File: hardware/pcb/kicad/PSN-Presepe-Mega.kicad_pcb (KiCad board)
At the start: 2 copper layers, 280 x 170 mm, 77 parts, among them J1 12V_IN, K1 G5Q-1_DC12, K10 G5Q-1_DC12, K11 G5Q-1_DC12, K12 G5Q-1_DC12, K13 G5Q-1_DC12, K14 G5Q-1_DC12, K15 G5Q-1_DC12, K16 G5Q-1_DC12, K2 G5Q-1_DC12, K3 G5Q-1_DC12, K4 G5Q-1_DC12, K5 G5Q-1_DC12, K6 G5Q-1_DC12, K7 G5Q-1_DC12, K8 G5Q-1_DC12, K9 G5Q-1_DC12, Q1 IRLZ44N_CIELO_R, Q2 IRLZ44N_CIELO_G, Q3 IRLZ44N_CIELO_B, Q4 IRLZ44N_TRAM_R, Q5 IRLZ44N_TRAM_G, Q6 IRLZ44N_TRAM_B, Q7 IRLZ44N_ALBA_R, Q8 IRLZ44N_ALBA_G, Q9 IRLZ44N_ALBA_B, U1 ULN2803C, U2 ULN2803C

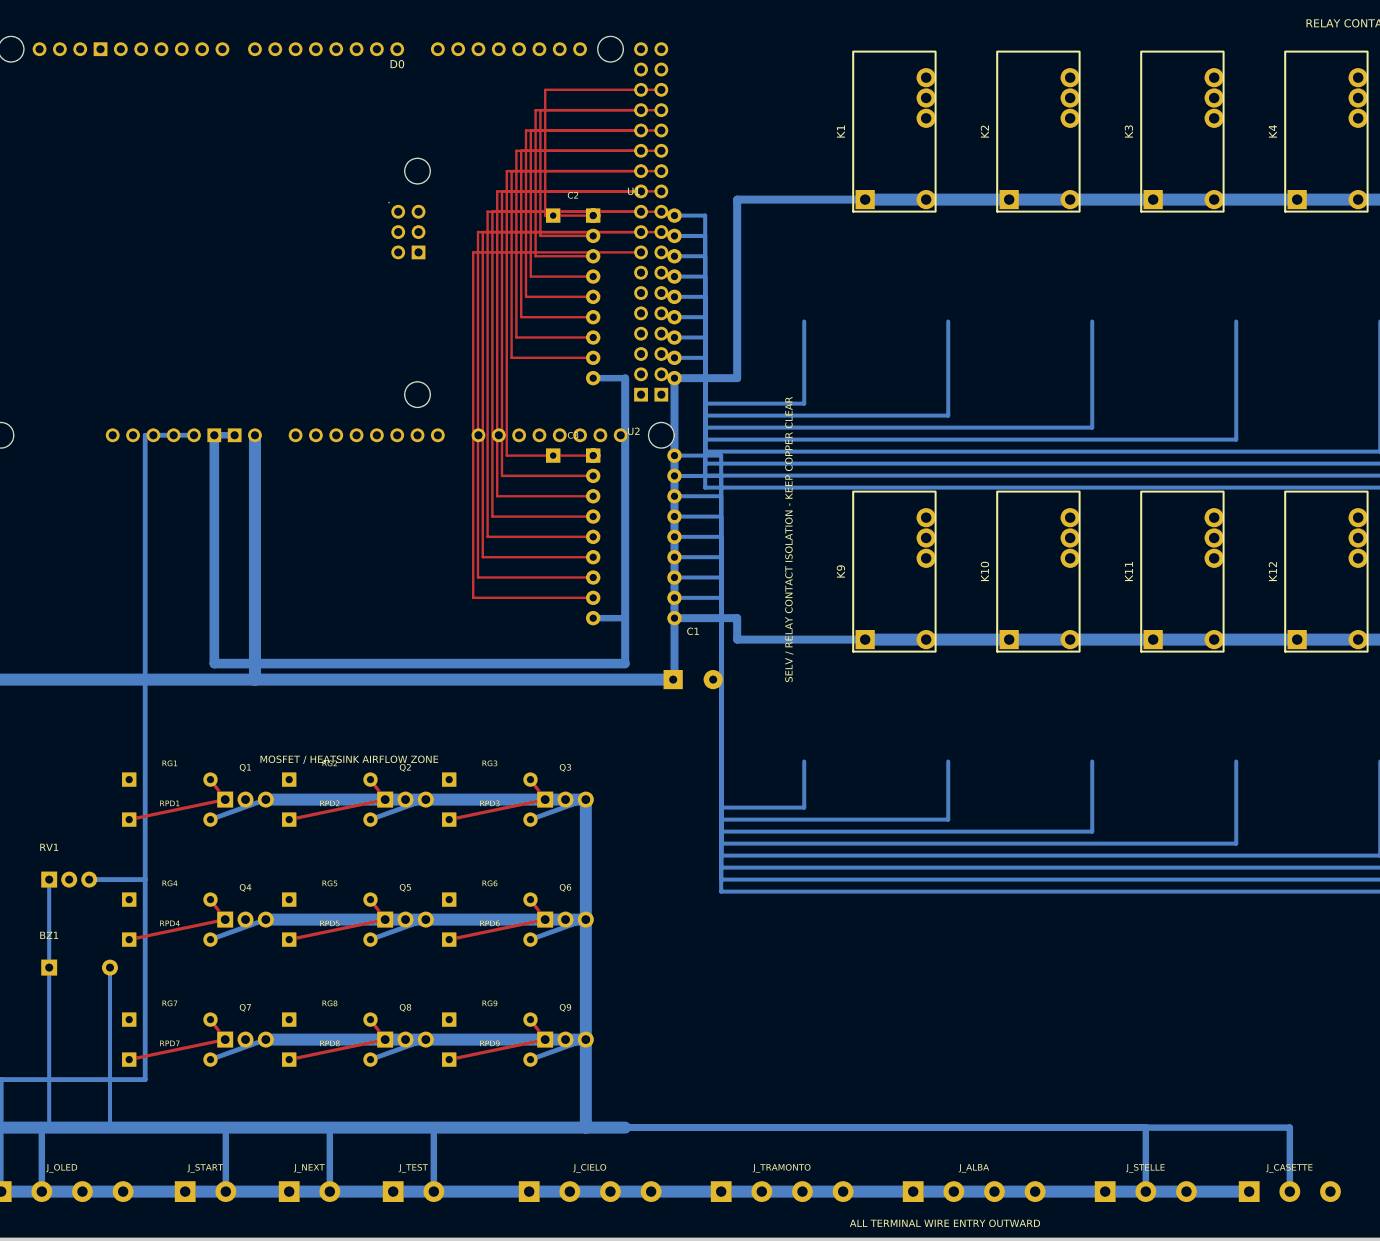
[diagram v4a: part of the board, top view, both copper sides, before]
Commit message: Route low-voltage controls and RGB PWM signals
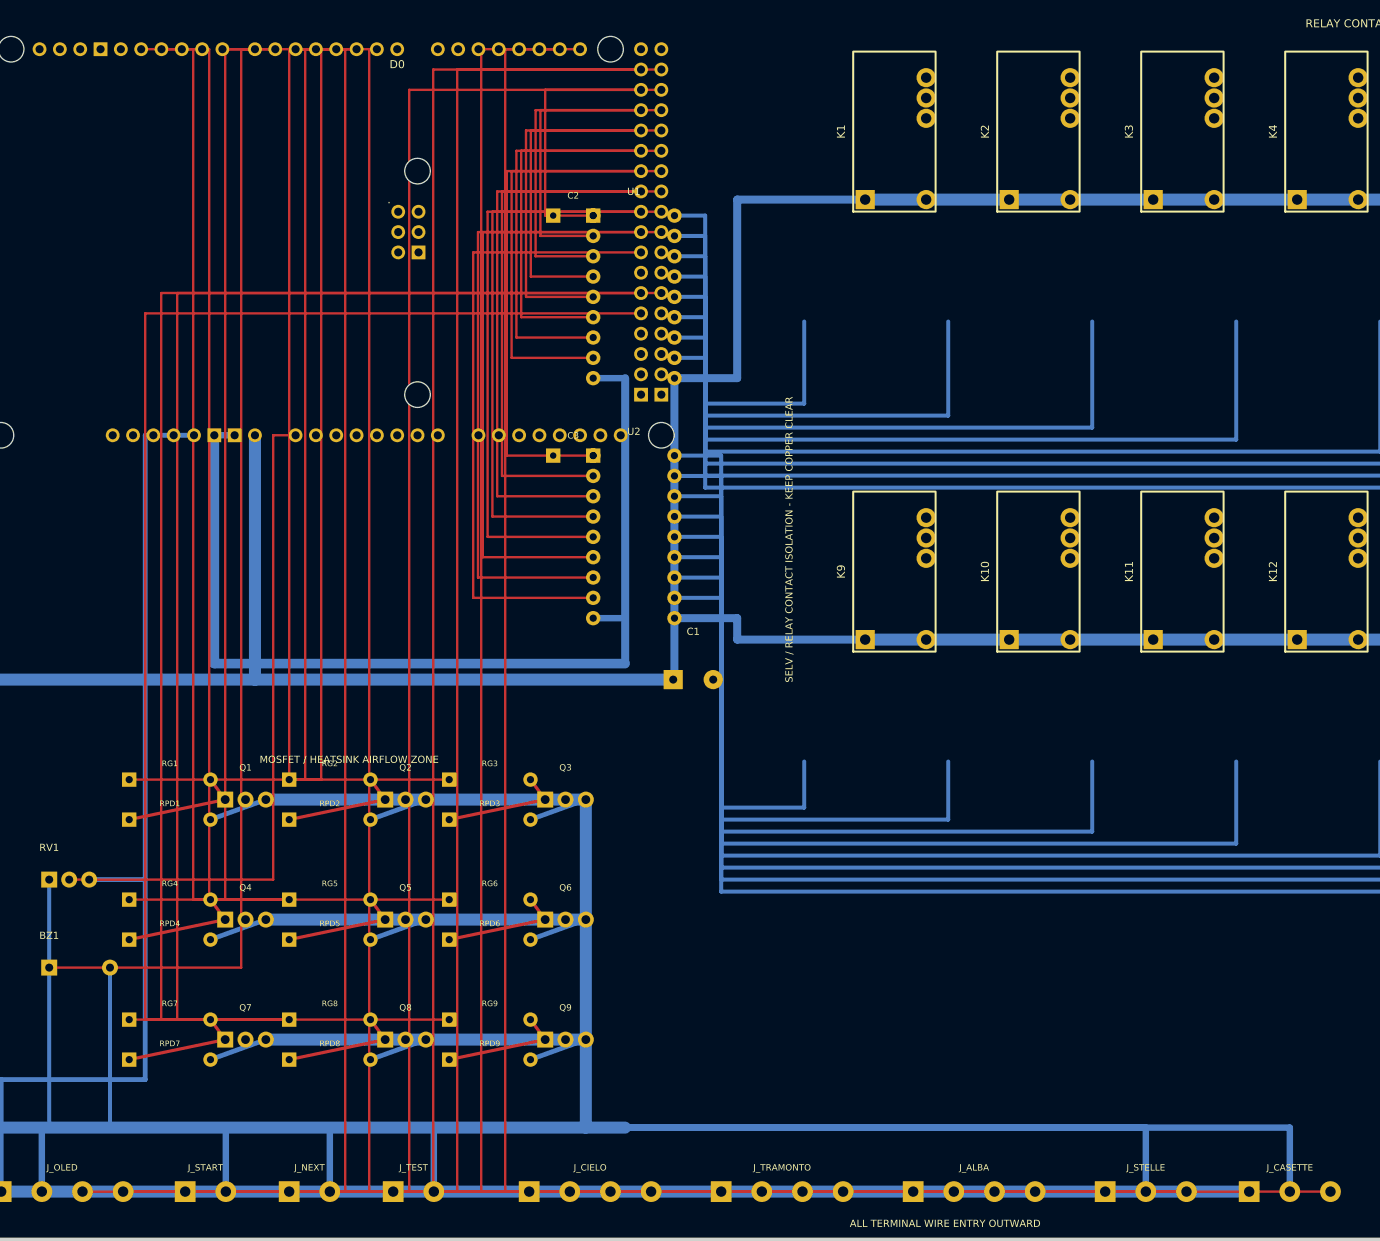
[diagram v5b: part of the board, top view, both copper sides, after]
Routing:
- net D8_CASETTE_DATA: track 0.00 -> 281.3 mm
- net D5_STELLE_DATA: track 0.00 -> 254.2 mm
- net D20_SDA: track 0.00 -> 202.5 mm
- net D21_SCL: track 0.00 -> 199.9 mm
- net D22_START: track 0.00 -> 197.2 mm
- net D46_ALBA_B: track 0.00 -> 188.3 mm
- net D23_NEXT: track 0.00 -> 186.8 mm
- net D45_ALBA_G: track 0.00 -> 169.3 mm
- net D24_TEST: track 0.00 -> 168.7 mm
- net D44_ALBA_R: track 0.00 -> 154.8 mm
- net D12_TRAM_B: track 0.00 -> 144.8 mm
- net D6_BUZZER: track 0.00 -> 143.1 mm
- net D11_TRAM_G: track 0.00 -> 122.3 mm
- net D7_TRAM_R: track 0.00 -> 122.0 mm
- net D2_CIELO_R: track 0.00 -> 119.7 mm
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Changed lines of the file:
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@@
   (segment (start 42 170) (end 42 184) (width 0.6) (layer "B.Cu") (net 52))
   (segment (start 68.64 89.46) (end 71.18 89.46) (width 0.8) (layer "B.Cu") (net 1))
+  (segment (start 111.82 41.2) (end 102 41.2) (width 0.3) (layer "F.Cu") (net 14))
+  (segment (start 102 41.2) (end 102 184) (width 0.3) (layer "F.Cu") (net 14))
+  (segment (start 102 184) (end 52.16 184) (width 0.3) (layer "F.Cu") (net 14))
+  (segment (start 114.36 41.2) (end 105 41.2) (width 0.3) (layer "F.Cu") (net 15))
+  (segment (start 105 41.2) (end 105 184) (width 0.3) (layer "F.Cu") (net 15))
+  (segment (start 105 184) (end 57.24 184) (width 0.3) (layer "F.Cu") (net 15))
+  (segment (start 121.98 43.74) (end 96 43.74) (width 0.3) (layer "F.Cu") (net 16))
+  (segment (start 96 43.74) (end 96 184) (width 0.3) (layer "F.Cu") (net 16))
+  (segment (start 96 184) (end 65 184) (width 0.3) (layer "F.Cu") (net 16))
+  (segment (start 124.52 43.74) (end 99 43.74) (width 0.3) (layer "F.Cu") (net 17))
+  (segment (start 99 43.74) (end 99 184) (width 0.3) (layer "F.Cu") (net 17))
+  (segment (start 99 184) (end 78 184) (width 0.3) (layer "F.Cu") (net 17))
+  (segment (start 121.98 46.28) (end 93 46.28) (width 0.3) (layer "F.Cu") (net 18))
+  (segment (start 93 46.28) (end 93 184) (width 0.3) (layer "F.Cu") (net 18))
+  (segment (start 93 184) (end 91 184) (width 0.3) (layer "F.Cu") (net 18))
+  (segment (start 78.8 41.2) (end 88 41.2) (width 0.3) (layer "F.Cu") (net 12))
+  (segment (start 88 41.2) (end 88 184) (width 0.3) (layer "F.Cu") (net 12))
+  (segment (start 88 184) (end 190.16 184) (width 0.3) (layer "F.Cu") (net 12))
+  (segment (start 69.66 41.2) (end 85 41.2) (width 0.3) (layer "F.Cu") (net 13))
+  (segment (start 85 41.2) (end 85 184) (width 0.3) (layer "F.Cu") (net 13))
+  (segment (start 85 184) (end 208.16 184) (width 0.3) (layer "F.Cu") (net 13))
+  (segment (start 78.8 89.46) (end 76 89.46) (width 0.3) (layer "F.Cu") (net 19))
+  (segment (start 76 89.46) (end 76 145) (width 0.3) (layer "F.Cu") (net 19))
+  (segment (start 76 145) (end 50.5 145) (width 0.3) (layer "F.Cu") (net 19))
+  (segment (start 76.26 41.2) (end 72 41.2) (width 0.3) (layer "F.Cu") (net 62))
+  (segment (start 72 41.2) (end 72 156) (width 0.3) (layer "F.Cu") (net 62))
+  (segment (start 72 156) (end 48 156) (width 0.3) (layer "F.Cu") (net 62))
+  (segment (start 86.42 41.2) (end 82 41.2) (width 0.3) (layer "F.Cu") (net 3))
+  (segment (start 82 41.2) (end 82 132.5) (width 0.3) (layer "F.Cu") (net 3))
+  (segment (start 82 132.5) (end 58 132.5) (width 0.3) (layer "F.Cu") (net 3))
+  (segment (start 83.88 41.2) (end 80 41.2) (width 0.3) (layer "F.Cu") (net 4))
+  (segment (start 80 41.2) (end 80 132.5) (width 0.3) (layer "F.Cu") (net 4))
+  (segment (start 80 132.5) (end 78 132.5) (width 0.3) (layer "F.Cu") (net 4))
+  (segment (start 81.34 41.2) (end 78 41.2) (width 0.3) (layer "F.Cu") (net 5))
+  (segment (start 78 41.2) (end 78 132.5) (width 0.3) (layer "F.Cu") (net 5))
+  (segment (start 78 132.5) (end 98 132.5) (width 0.3) (layer "F.Cu") (net 5))
+  (segment (start 73.72 41.2) (end 70 41.2) (width 0.3) (layer "F.Cu") (net 6))
+  (segment (start 70 41.2) (end 70 147.5) (width 0.3) (layer "F.Cu") (net 6))
+  (segment (start 70 147.5) (end 58 147.5) (width 0.3) (layer "F.Cu") (net 6))
+  (segment (start 62.04 41.2) (end 68 41.2) (width 0.3) (layer "F.Cu") (net 7))
+  (segment (start 68 41.2) (end 68 147.5) (width 0.3) (layer "F.Cu") (net 7))
+  (segment (start 68 147.5) (end 78 147.5) (width 0.3) (layer "F.Cu") (net 7))
+  (segment (start 59.5 41.2) (end 66 41.2) (width 0.3) (layer "F.Cu") (net 8))
+  (segment (start 66 41.2) (end 66 147.5) (width 0.3) (layer "F.Cu") (net 8))
+  (segment (start 66 147.5) (end 98 147.5) (width 0.3) (layer "F.Cu") (net 8))
+  (segment (start 121.98 71.68) (end 64 71.68) (width 0.3) (layer "F.Cu") (net 9))
+  (segment (start 64 71.68) (end 64 162.5) (width 0.3) (layer "F.Cu") (net 9))
+  (segment (start 64 162.5) (end 58 162.5) (width 0.3) (layer "F.Cu") (net 9))
+  (segment (start 124.52 71.68) (end 62 71.68) (width 0.3) (layer "F.Cu") (net 10))
+  (segment (start 62 71.68) (end 62 162.5) (width 0.3) (layer "F.Cu") (net 10))
+  (segment (start 62 162.5) (end 78 162.5) (width 0.3) (layer "F.Cu") (net 10))
+  (segment (start 121.98 74.22) (end 60 74.22) (width 0.3) (layer "F.Cu") (net 11))
+  (segment (start 60 74.22) (end 60 162.5) (width 0.3) (layer "F.Cu") (net 11))
+  (segment (start 60 162.5) (end 98 162.5) (width 0.3) (layer "F.Cu") (net 11))
 )

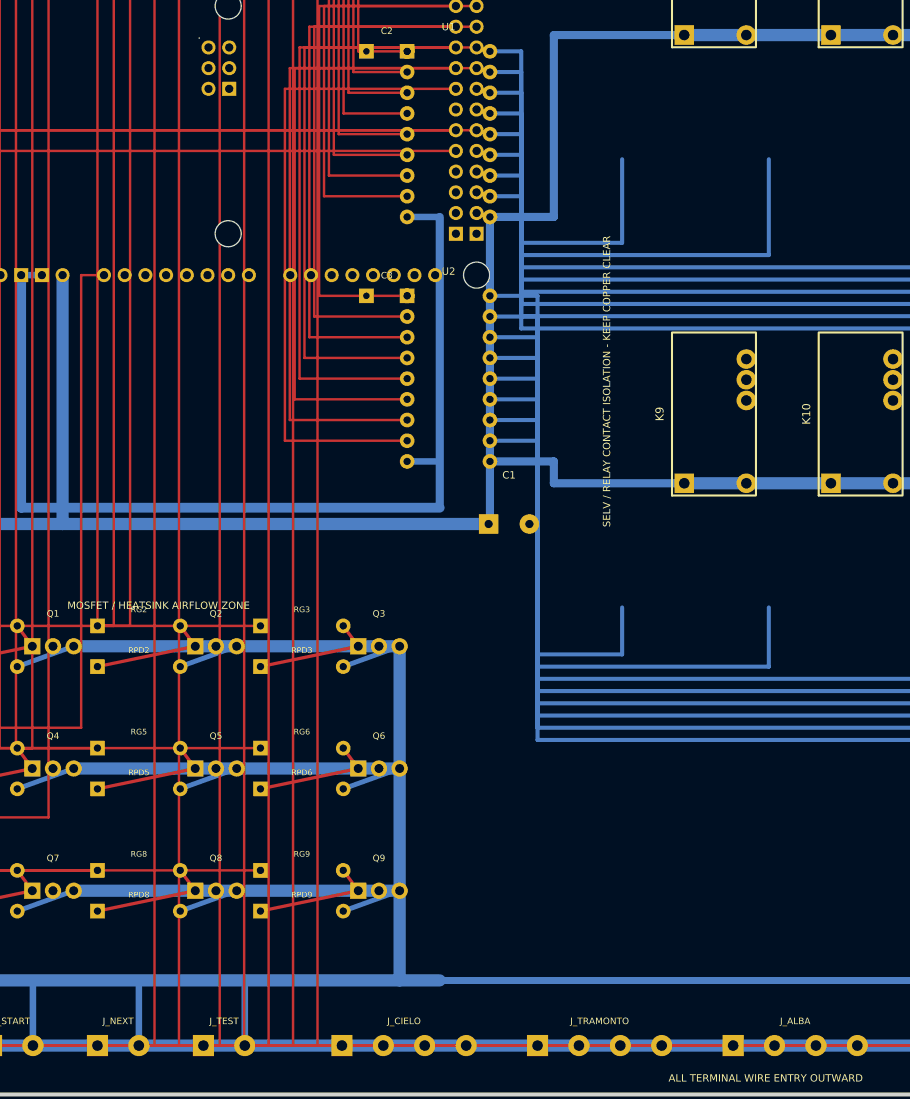
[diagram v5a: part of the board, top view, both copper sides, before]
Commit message: Route RGB load outputs and power filtering
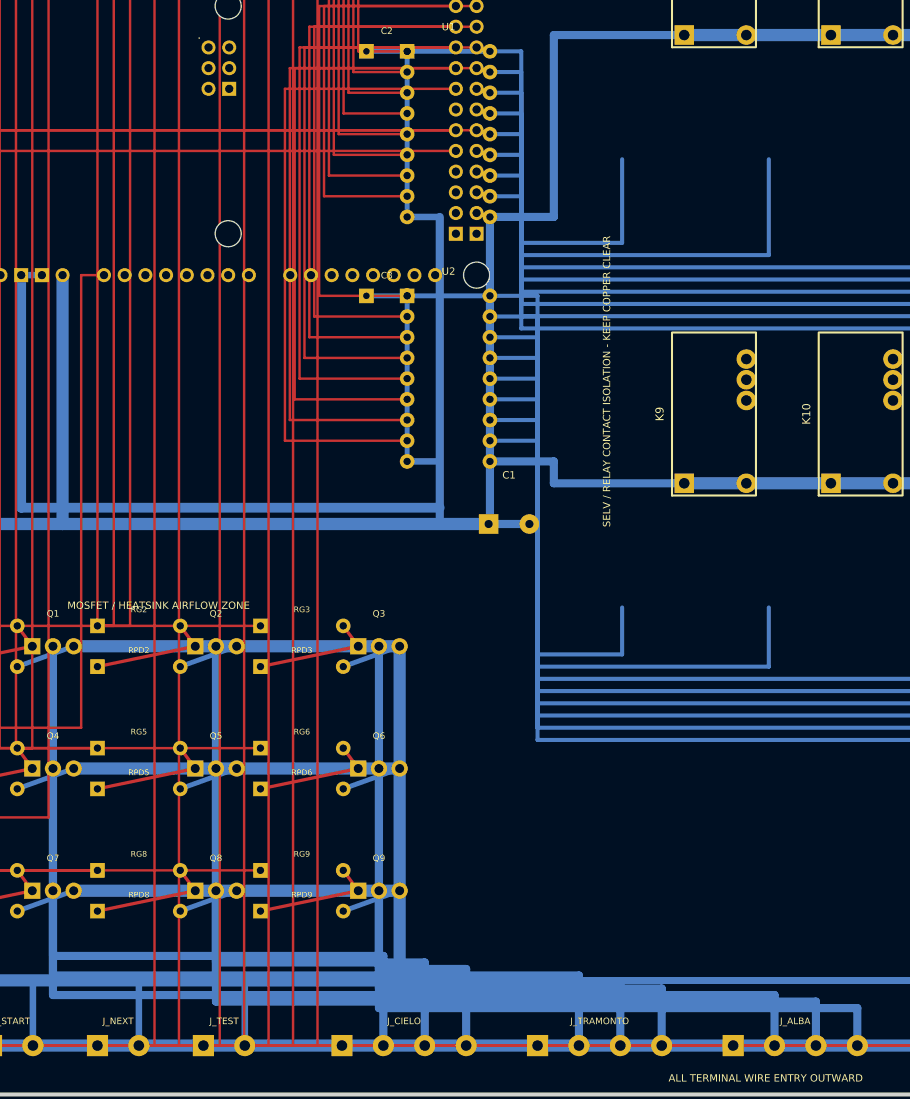
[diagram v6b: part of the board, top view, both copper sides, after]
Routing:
- net ALBA_R_NEG: track 0.00 -> 107.5 mm
- net TRAM_R_NEG: track 0.00 -> 98.5 mm
- net ALBA_G_NEG: track 0.00 -> 92.6 mm
- net CIELO_R_NEG: track 0.00 -> 89.5 mm
- net TRAM_G_NEG: track 0.00 -> 83.6 mm
- net ALBA_B_NEG: track 0.00 -> 77.7 mm
- net CIELO_G_NEG: track 0.00 -> 74.6 mm
- net TRAM_B_NEG: track 0.00 -> 68.7 mm
- net CIELO_B_NEG: track 0.00 -> 59.7 mm
- net GND: track 1033.3 -> 1086.9 mm
- net +12V: track 725.1 -> 755.5 mm
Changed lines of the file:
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@@
   (segment (start 60 74.22) (end 60 162.5) (width 0.3) (layer "F.Cu") (net 11))
   (segment (start 60 162.5) (end 98 162.5) (width 0.3) (layer "F.Cu") (net 11))
+  (segment (start 72.54 135) (end 72.54 173) (width 1.0) (layer "B.Cu") (net 53))
+  (segment (start 72.54 173) (end 113.08 173) (width 1.0) (layer "B.Cu") (net 53))
+  (segment (start 113.08 173) (end 113.08 184) (width 1.0) (layer "B.Cu") (net 53))
+  (segment (start 92.54 135) (end 92.54 173.8) (width 1.0) (layer "B.Cu") (net 54))
+  (segment (start 92.54 173.8) (end 118.16 173.8) (width 1.0) (layer "B.Cu") (net 54))
+  (segment (start 118.16 173.8) (end 118.16 184) (width 1.0) (layer "B.Cu") (net 54))
+  (segment (start 112.54 135) (end 112.54 174.6) (width 1.0) (layer "B.Cu") (net 55))
+  (segment (start 112.54 174.6) (end 123.24 174.6) (width 1.0) (layer "B.Cu") (net 55))
+  (segment (start 123.24 174.6) (end 123.24 184) (width 1.0) (layer "B.Cu") (net 55))
+  (segment (start 72.54 150) (end 72.54 175.4) (width 1.0) (layer "B.Cu") (net 56))
+  (segment (start 72.54 175.4) (end 137.08 175.4) (width 1.0) (layer "B.Cu") (net 56))
+  (segment (start 137.08 175.4) (end 137.08 184) (width 1.0) (layer "B.Cu") (net 56))
+  (segment (start 92.54 150) (end 92.54 176.2) (width 1.0) (layer "B.Cu") (net 57))
+  (segment (start 92.54 176.2) (end 142.16 176.2) (width 1.0) (layer "B.Cu") (net 57))
+  (segment (start 142.16 176.2) (end 142.16 184) (width 1.0) (layer "B.Cu") (net 57))
+  (segment (start 112.54 150) (end 112.54 177) (width 1.0) (layer "B.Cu") (net 58))
+  (segment (start 112.54 177) (end 147.24 177) (width 1.0) (layer "B.Cu") (net 58))
+  (segment (start 147.24 177) (end 147.24 184) (width 1.0) (layer "B.Cu") (net 58))
+  (segment (start 72.54 165) (end 72.54 177.8) (width 1.0) (layer "B.Cu") (net 59))
+  (segment (start 72.54 177.8) (end 161.08 177.8) (width 1.0) (layer "B.Cu") (net 59))
+  (segment (start 161.08 177.8) (end 161.08 184) (width 1.0) (layer "B.Cu") (net 59))
+  (segment (start 92.54 165) (end 92.54 178.6) (width 1.0) (layer "B.Cu") (net 60))
+  (segment (start 92.54 178.6) (end 166.16 178.6) (width 1.0) (layer "B.Cu") (net 60))
+  (segment (start 166.16 178.6) (end 166.16 184) (width 1.0) (layer "B.Cu") (net 60))
+  (segment (start 112.54 165) (end 112.54 179.4) (width 1.0) (layer "B.Cu") (net 61))
+  (segment (start 112.54 179.4) (end 171.24 179.4) (width 1.0) (layer "B.Cu") (net 61))
+  (segment (start 171.24 179.4) (end 171.24 184) (width 1.0) (layer "B.Cu") (net 61))
+  (segment (start 126 120) (end 126.16 120) (width 1.0) (layer "B.Cu") (net 2))
+  (segment (start 131 120) (end 120 120) (width 1.0) (layer "B.Cu") (net 1))
+  (segment (start 120 120) (end 120 118) (width 1.0) (layer "B.Cu") (net 1))
+  (segment (start 111 62) (end 126.16 62) (width 0.6) (layer "B.Cu") (net 2))
+  (segment (start 116 62) (end 116 82.32) (width 0.6) (layer "B.Cu") (net 1))
+  (segment (start 111 92) (end 126.16 92) (width 0.6) (layer "B.Cu") (net 2))
+  (segment (start 116 92) (end 116 112.32) (width 0.6) (layer "B.Cu") (net 1))
 )
